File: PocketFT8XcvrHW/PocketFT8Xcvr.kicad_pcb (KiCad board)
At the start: 4 copper layers, 101.6 x 69.9 mm, 60 parts, among them J1 HX8357D SPI, J2 22-23-2021, J3 GPS, J5 HX8357D 8-BIT, Q1 2N3904, Q2 2N3906, Q3 2N7000, Q4 2N7000, U1 MCP3422A1T-E/SN, U2 Si4735-D60-GU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

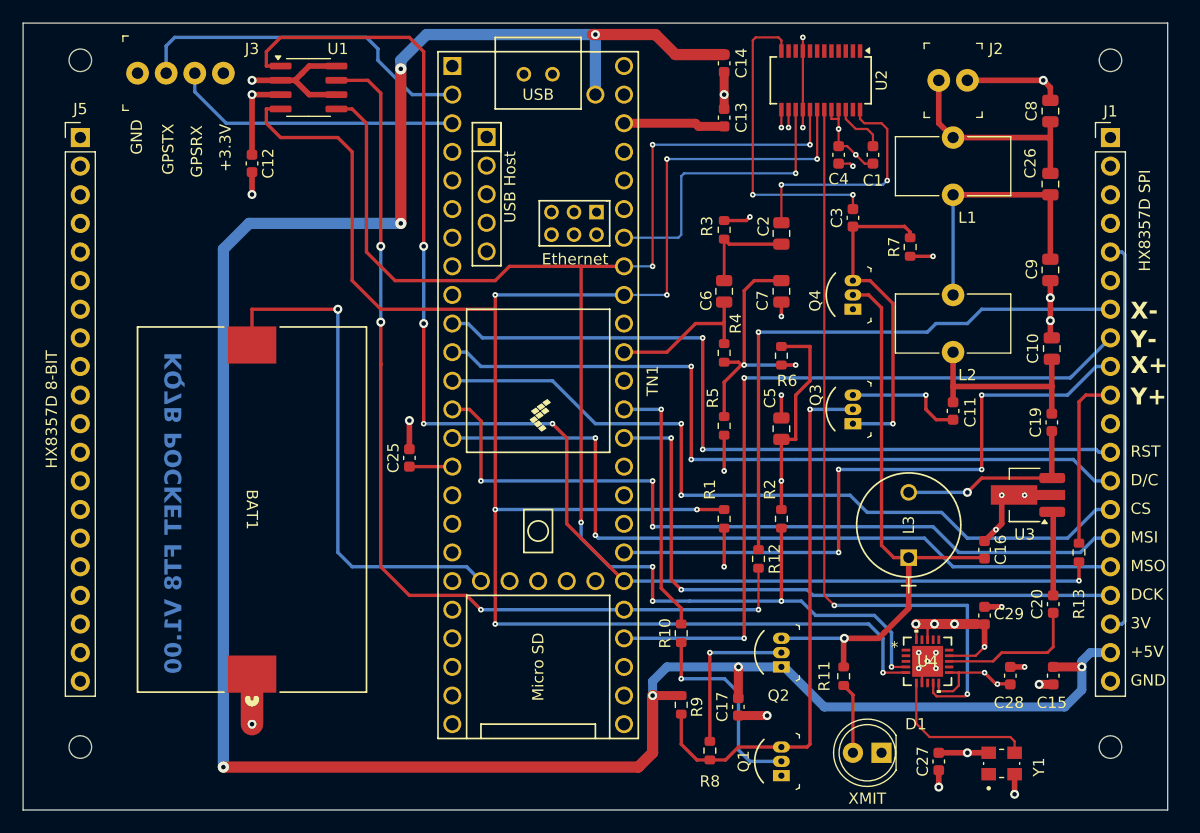
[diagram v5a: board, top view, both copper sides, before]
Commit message: Cost down on PCB for V1.10
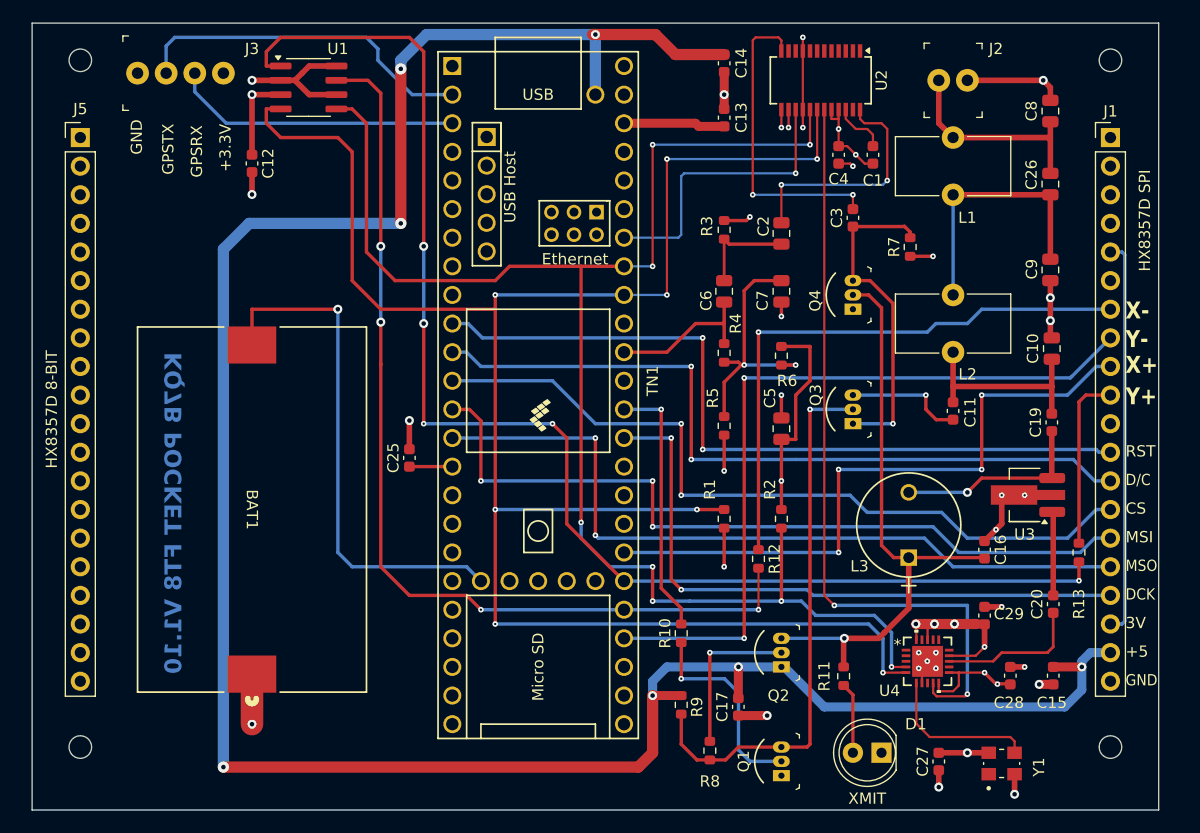
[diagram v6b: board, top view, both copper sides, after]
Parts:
- C10, C8: value 75PF -> 910pf
- C9: value 243PF -> 1300pf
- L1, L2: value 0.5uH -> 1.2uh
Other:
- board size 101.6 x 69.9 mm -> 100 x 69.9 mm
- board text added: "+5"
- board text added: "KQ7B POCKET FT8 V1.10"
- board text removed: "+5V"
- board text removed: "KQ7B POCKET FT8 V1.00"

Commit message: Moved battery to back (solder) side of board
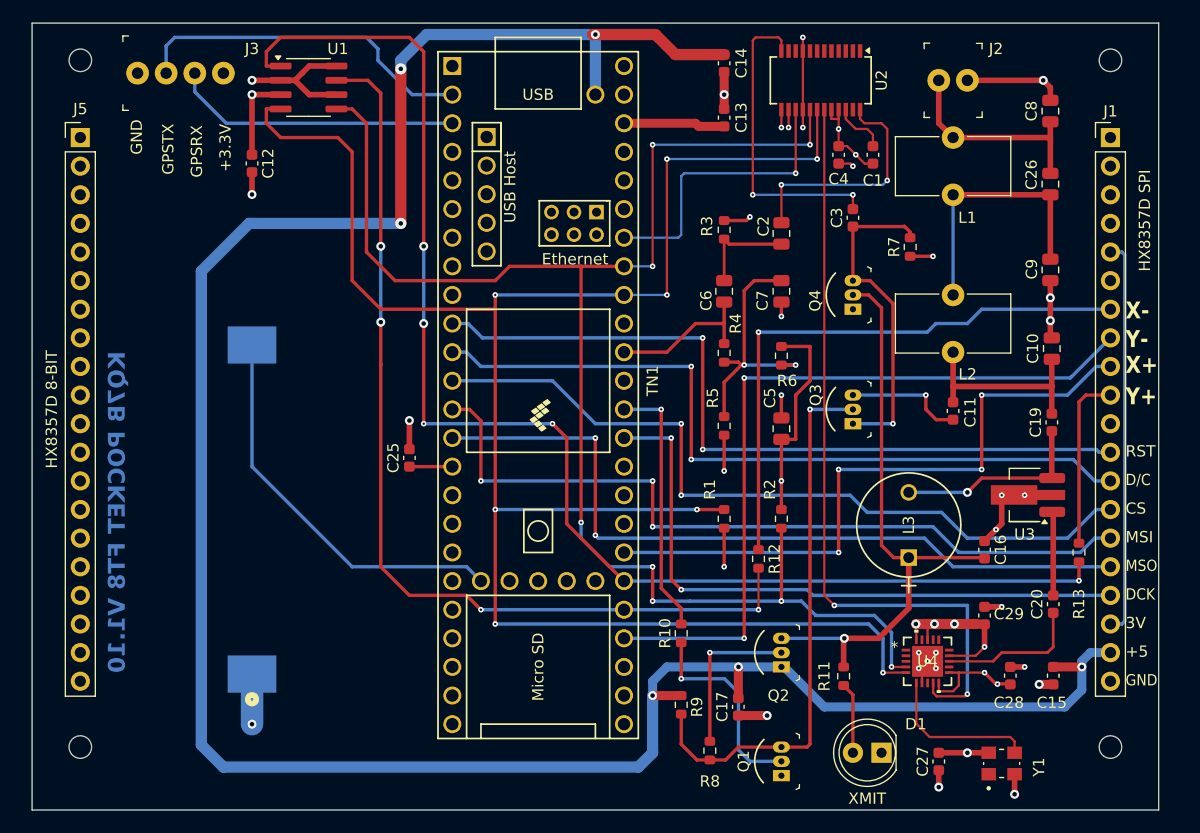
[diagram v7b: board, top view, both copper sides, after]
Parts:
- BAT1: moved to B.Cu
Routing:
- net Net-(TN1-VBAT): track 46.1 -> 35.3 mm, vias 1 -> 0
- net +5V: track 211.8 -> 213.4 mm, vias 7 -> 6

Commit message: Revise GPS Connector
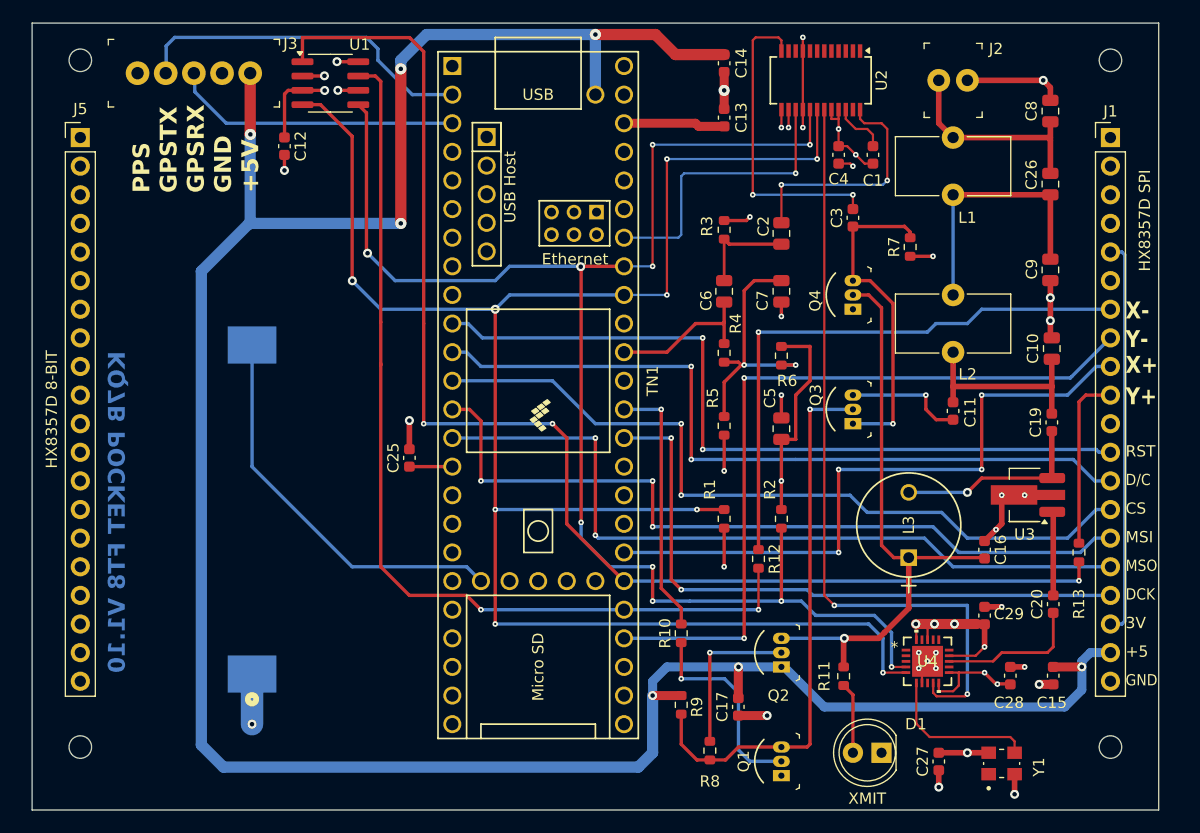
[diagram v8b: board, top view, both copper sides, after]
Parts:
- J3: value GPS -> B5B-XH-A_LF__SN_; footprint digikey-footprints:PinHeader_1x4_P2.54mm_Drill1.02mm -> digikey-footprints:PinHeader_1x5_P2.5mm_Drill1.1mm
- moved C12 3.26 mm to (124.8, 61.7)
- moved U1 1.98 mm to (128.9, 56.1)
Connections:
- J3 pad 1: GND -> unconnected-(J3-PPS__-Pad1)
- J3 pad 4: +3.3V -> GND
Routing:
- net +5V: track 213.4 -> 226.6 mm, vias 6 -> 7
- net GND: track 80.0 -> 73.0 mm, vias 32 -> 34
- net /SDA: track 171.0 -> 166.0 mm, vias 8 -> 9
- net /Y+: track 120.8 -> 116.6 mm, vias 5 -> 3
- net /SCL: track 137.2 -> 136.0 mm, vias 8 -> 10
- net /X-: track 85.4 -> 84.2 mm, vias 4 -> 2
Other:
- board text added: "PPS GPSTX GPSRX GND +5V"
- board text removed: "+3.3V"
- board text removed: "GPSRX"
- board text removed: "GPSTX"
